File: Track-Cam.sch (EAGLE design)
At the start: 41 parts, among them IC1 STM32F042KT/M, IC2 BD6211F/M, IC3 BD6211F/M, P1 RASPI_BOARD_B+#_HC

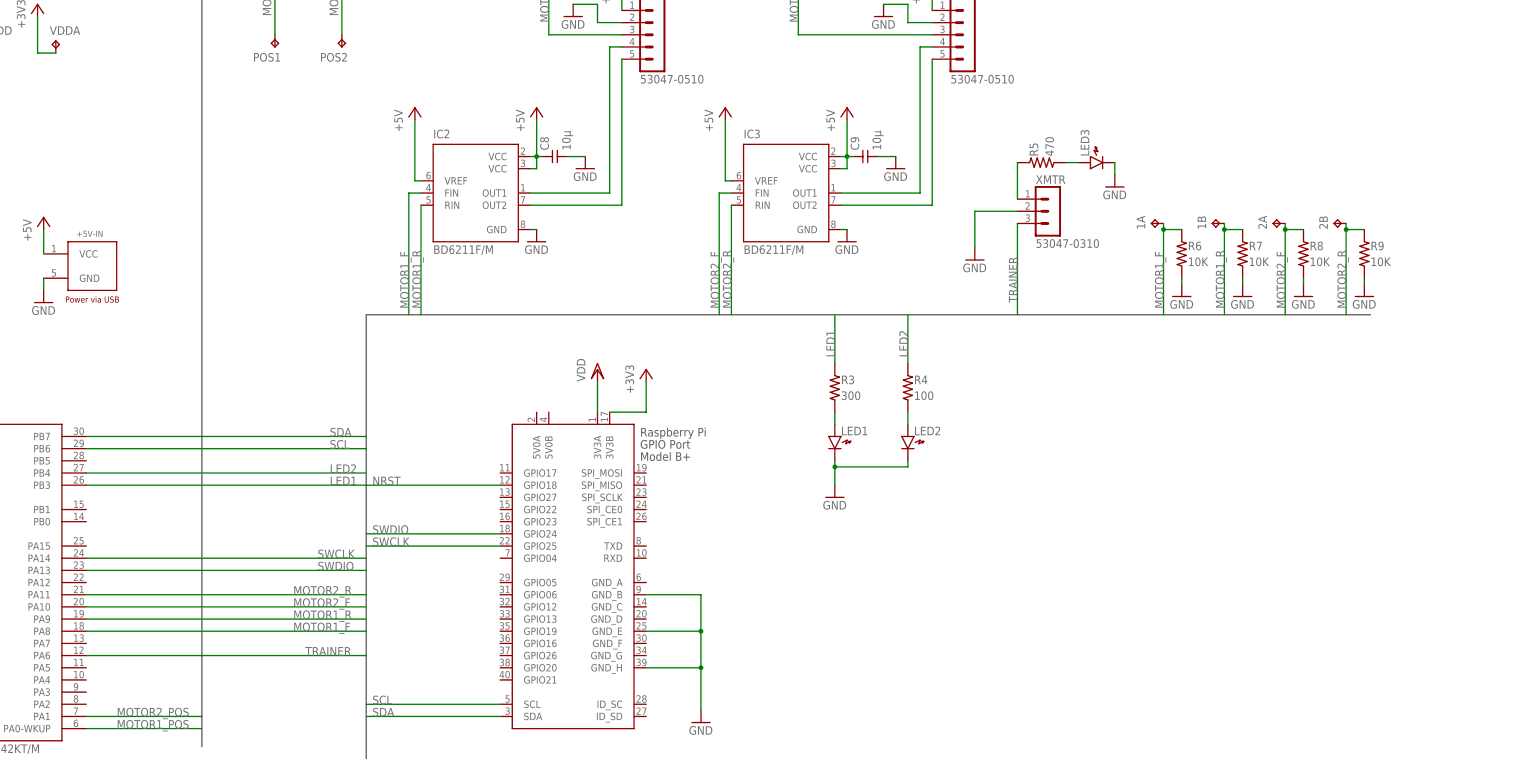
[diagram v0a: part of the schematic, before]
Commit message: fix 5v line bug
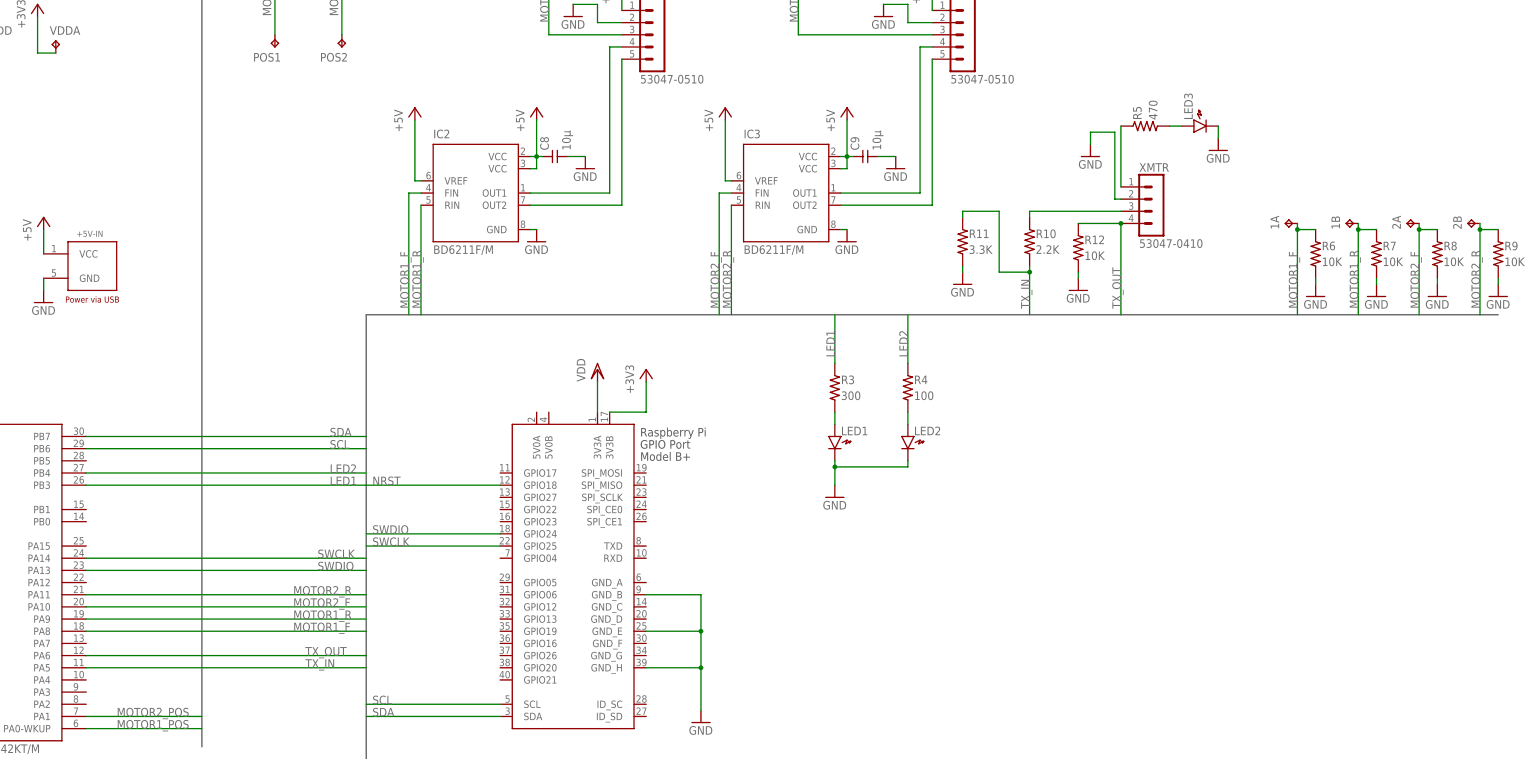
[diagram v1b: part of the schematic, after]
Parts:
- added R10: 2.2K, gen-discrete:RESISTOR-US2012
- added R11: 3.3K, gen-discrete:RESISTOR-US2012
- added R12: 10K, gen-discrete:RESISTOR-US2012
- XMTR: value 53047-0310 -> 53047-0410; device connector:53047-0310 -> connector:53047-0410
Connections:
- removed net TRAINER: IC1MCU.PA6, XMTR.3
- new net TX_IN: IC1MCU.PA5, R10.2, R11.1
- new net TX_IN_5V: R10.1, XMTR.3
- new net TX_OUT: IC1MCU.PA6, R12.1, XMTR.4
- net GND: now also R11.2, R12.2
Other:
- moved on the sheet: 1A, 1B, 2A, 2B, LED3, R5, R6, R7, R8, R9

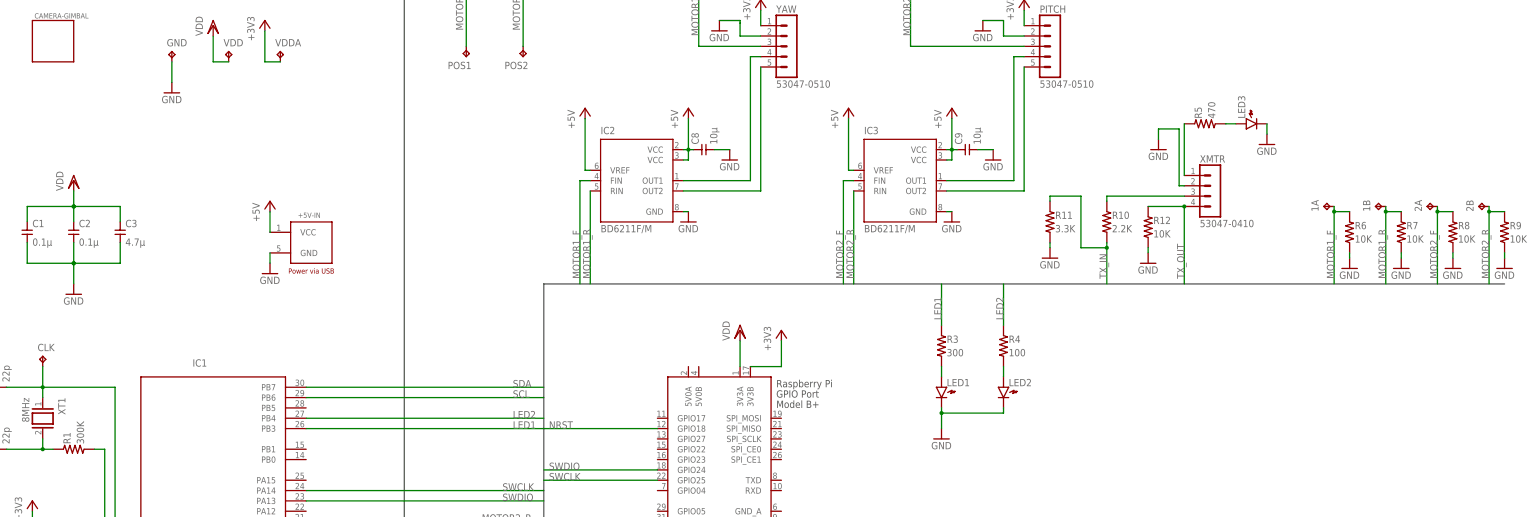
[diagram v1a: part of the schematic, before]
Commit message: fix BOM for 1st production
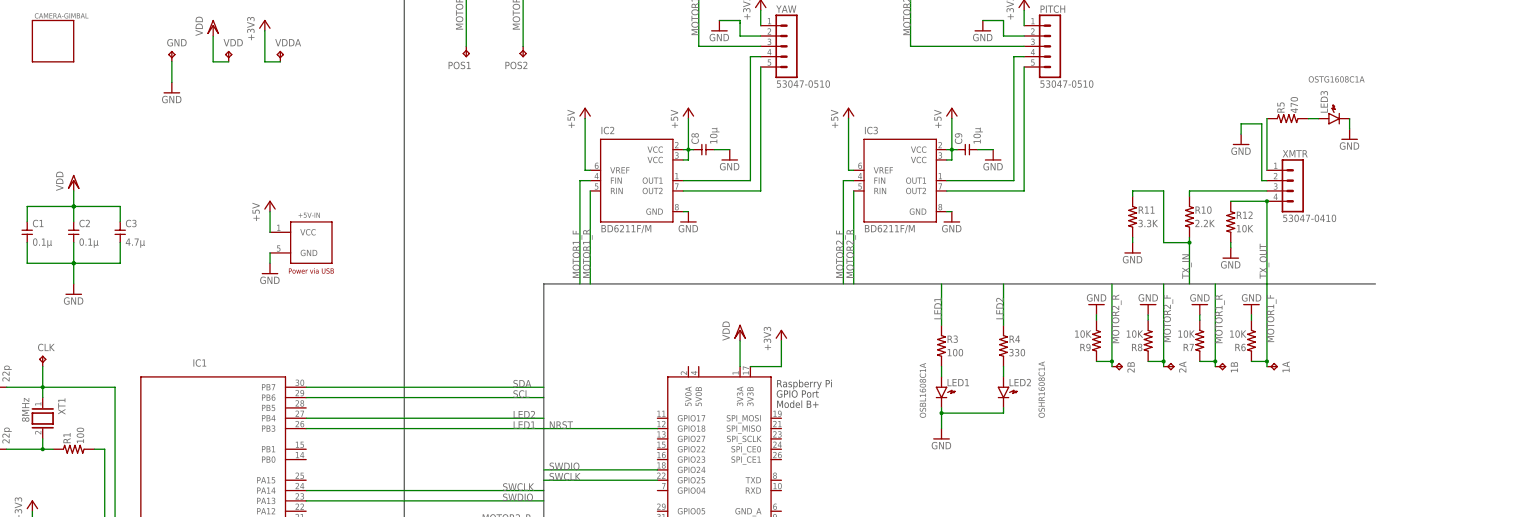
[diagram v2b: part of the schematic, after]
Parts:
- R1: value 300K -> 100
- R3: value 300 -> 100
- R4: value 100 -> 330
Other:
- note added: "OSBL1608C1A"
- note added: "OSHR1608C1A"
- note added: "OSTG1608C1A"
- moved on the sheet: 1A, 1B, 2A, 2B, LED3, R10, R11, R12, R5, R6, R7, R8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
